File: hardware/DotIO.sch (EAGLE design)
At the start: 37 parts, among them CN1 1X4-BIG, U1 ATMEGA328P-MU-QFN32, X1 S4B-ZR, X2 S4B-ZR, X3 S4B-ZR, X4 S4B-ZR, X5 S4B-ZR, X6 S4B-ZR, X7 S4B-ZR

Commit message: Initial routing
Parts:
- removed LED5, LED6, LED7, LED8: (no value), SparkFun:LED0603
- removed X2: S4B-ZR, con-jst:S4B-ZR
- added C1, C9: 1uF, rcl:C-EUC0603
- added D1, D2: (no value), diode:DIODE-SOD523
- added IC2: (no value), MCP1700:MCP1700TT
- added J3: USB-MICROB, SparkFun-Retired:USB-MICROB
- added R6: 68Ω, rcl:R-EU_R0603
- added R8: 1.5kΩ, rcl:R-EU_R0603
- R2: value 150Ω -> 68Ω; device SparkFun:RESISTOR-ARRAY0603-ARV -> rcl:R-EU_R0603
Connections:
- net LED renamed RGB_RED
- removed net ADCENA: U1.PB1(OC1A/PCINT1)
- removed net CS_FLASH: U1.PC0(ADC0/PCINT8)
- removed net N$11: LED6.C, R2A.1
- removed net N$12: LED7.C, R2B.1
- removed net N$13: LED8.C, R2D.1
- removed net N$3: LED5.C, R2C.1
- removed net OUTA: LED11.A, LED3.A, LED5.A, LED6.A, U1.PB2(SS/OC1B/PCINT2), X1-3.1, X2-3.1, X3-3.1, X5-3.1
- removed net OUTB: LED12.A, LED4.A, LED7.A, LED8.A, X1-2.1, X2-2.1, X3-2.1, X5-2.1
- removed net RSEL: U1.PC3(ADC3/PCINT11)
- removed net RXD: R1C.1
- removed net TXD: R1B.1
- new net 4_0: LED11.A, U1.PC0(ADC0/PCINT8), X5-3.1
- new net 4_1: LED12.A, U1.PC1(ADC1PCINT9), X5-2.1
- new net 5_0: LED3.A, U1.PC2(ADC2PCINT10), X3-3.1
- new net 5_1: LED4.A, U1.PC3(ADC3/PCINT11), X3-2.1
- new net RGB_BLUE: R1C.1, U1.PB2(SS/OC1B/PCINT2)
- new net RGB_GREEN: R1B.1, U1.PB1(OC1A/PCINT1)
- new net USB_D+: D2.C, J3.D+, R2.1
- new net USB_D-: D1.C, J3.D-, R6.1, R8.1
- net +3V3: now also C1.1, IC2.OUT, R8.2, X1-3.1
- net +5V: now also C9.1, IC2.IN, J3.VBUS; no longer X1-4.1, X2-4.1
- net D+: now also R2.2; no longer U1.PC2(ADC2PCINT10)
- net D-: now also R6.2; no longer U1.PC1(ADC1PCINT9)
- net GND: now also C1.2, C9.2, D1.A, D2.A, IC2.GND, J3.GND, X1-4.1; no longer R2A.2, R2B.2, R2C.2, R2D.2, X1-1.1, X2-1.1
- net SCL: now also X1-2.1
- net SDA: now also X1-1.1
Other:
- moved on the sheet: X1-1, X1-2, X1-3, X1-4

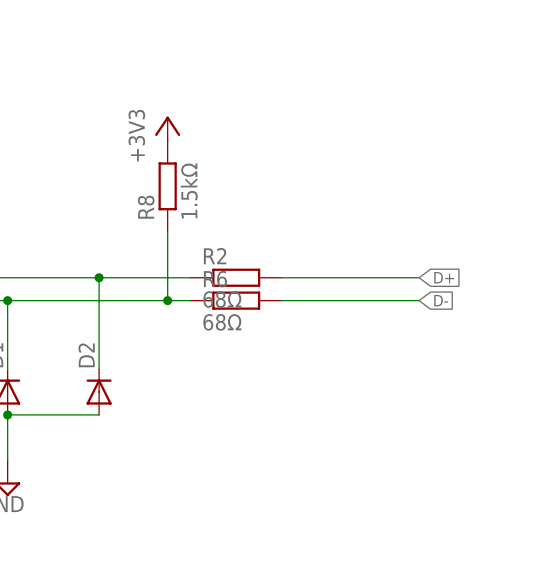
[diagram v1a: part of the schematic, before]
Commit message: Bind USB to SPI pins
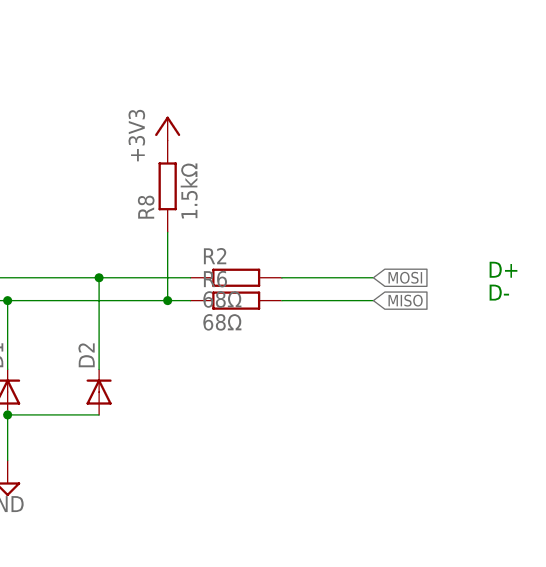
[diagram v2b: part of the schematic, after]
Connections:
- removed net D+: R2.2
- removed net D-: R6.2
- net MISO: now also R6.2
- net MOSI: now also R2.2
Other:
- note added: "D+"
- note added: "D-"
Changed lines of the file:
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@@
 <setting verticaltext="up"/>
 </settings>
-<grid distance="0.05" unitdist="inch" unit="inch" style="lines" multiple="1" display="no" altdistance="0.01" altunitdist="inch" altunit="inch"/>
+<grid distance="0.1" unitdist="inch" unit="inch" style="lines" multiple="1" display="no" altdistance="0.01" altunitdist="inch" altunit="inch"/>
 <layers>
 <layer number="1" name="Top" color="4" fill="1" visible="no" active="no"/>
@@
 <text x="196.85" y="213.36" size="1.778" layer="91">white</text>
 <text x="196.85" y="203.2" size="1.778" layer="91">red</text>
+<text x="381" y="144.78" size="1.778" layer="91">D+</text>
+<text x="381" y="142.24" size="1.778" layer="91">D-</text>
 </plain>
 <instances>
@@
 <label x="52.07" y="125.73" size="1.27" layer="95" rot="R180" xref="yes"/>
 </segment>
+<segment>
+<pinref part="R2" gate="G$1" pin="2"/>
+<wire x1="358.14" y1="144.78" x2="368.3" y2="144.78" width="0.1524" layer="91"/>
+<label x="368.3" y="144.78" size="1.27" layer="95" xref="yes"/>
+</segment>
 </net>
 <net name="MISO" class="0">
@@
 <wire x1="60.96" y1="123.19" x2="52.07" y2="123.19" width="0.1524" layer="91"/>
 <label x="52.07" y="123.19" size="1.27" layer="95" rot="R180" xref="yes"/>
+</segment>
+<segment>
+<pinref part="R6" gate="G$1" pin="2"/>
+<wire x1="358.14" y1="142.24" x2="368.3" y2="142.24" width="0.1524" layer="91"/>
+<label x="368.3" y="142.24" size="1.27" layer="95" xref="yes"/>
 </segment>
 </net>
@@
 </segment>
 </net>
-<net name="D-" class="0">
-<segment>
-<pinref part="R6" gate="G$1" pin="2"/>
-<wire x1="358.14" y1="142.24" x2="373.38" y2="142.24" width="0.1524" layer="91"/>
-<label x="373.38" y="142.24" size="1.27" layer="95" xref="yes"/>
-</segment>
-</net>
-<net name="D+" class="0">
-<segment>
-<pinref part="R2" gate="G$1" pin="2"/>
-<wire x1="358.14" y1="144.78" x2="373.38" y2="144.78" width="0.1524" layer="91"/>
-<label x="373.38" y="144.78" size="1.27" layer="95" xref="yes"/>
-</segment>
-</net>

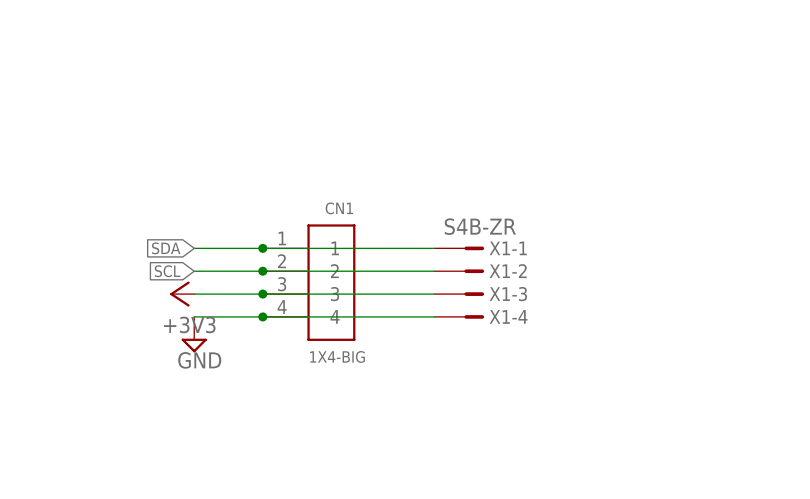
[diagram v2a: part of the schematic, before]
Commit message: Flip I2C JST port
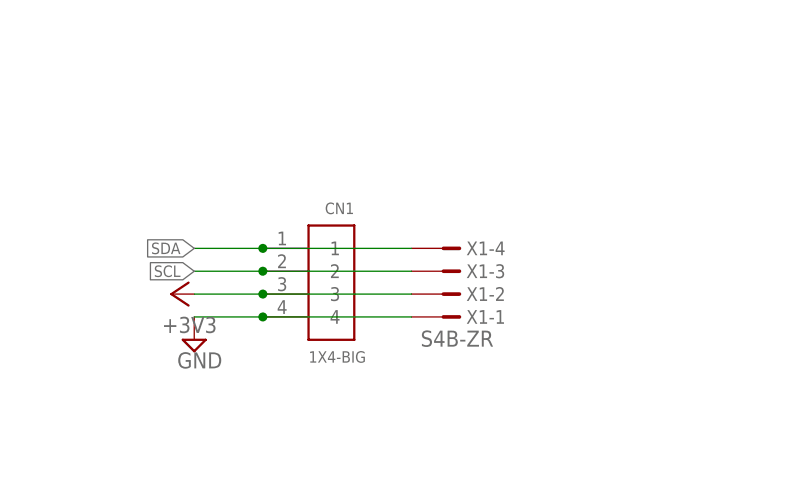
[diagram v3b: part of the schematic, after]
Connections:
- net +3V3: now also X1-2.1; no longer X1-3.1
- net GND: now also X1-1.1; no longer X1-4.1
- net SCL: now also X1-3.1; no longer X1-2.1
- net SDA: now also X1-4.1; no longer X1-1.1
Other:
- moved on the sheet: X1-1, X1-2, X1-3, X1-4
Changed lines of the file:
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@@
 <setting verticaltext="up"/>
 </settings>
-<grid distance="0.1" unitdist="inch" unit="inch" style="lines" multiple="1" display="no" altdistance="0.01" altunitdist="inch" altunit="inch"/>
+<grid distance="0.05" unitdist="inch" unit="inch" style="lines" multiple="1" display="no" altdistance="0.01" altunitdist="inch" altunit="inch"/>
 <layers>
 <layer number="1" name="Top" color="4" fill="1" visible="no" active="no"/>
@@
 <instance part="SUPPLY10" gate="GND" x="269.24" y="88.9"/>
 <instance part="J3" gate="G$1" x="279.4" y="99.06"/>
-<instance part="X1" gate="-1" x="100.33" y="-72.39"/>
-<instance part="X1" gate="-2" x="100.33" y="-74.93"/>
-<instance part="X1" gate="-3" x="100.33" y="-77.47"/>
-<instance part="X1" gate="-4" x="100.33" y="-80.01"/>
+<instance part="X1" gate="-1" x="97.79" y="-80.01" rot="MR180"/>
+<instance part="X1" gate="-2" x="97.79" y="-77.47" rot="MR180"/>
+<instance part="X1" gate="-3" x="97.79" y="-74.93" rot="MR180"/>
+<instance part="X1" gate="-4" x="97.79" y="-72.39" rot="MR180"/>
 </instances>
 <busses>
@@
 <wire x1="76.2" y1="-80.01" x2="68.58" y2="-80.01" width="0.1524" layer="91"/>
 <pinref part="SUPPLY11" gate="GND" pin="GND"/>
-<pinref part="X1" gate="-4" pin="1"/>
-<wire x1="76.2" y1="-80.01" x2="95.25" y2="-80.01" width="0.1524" layer="91"/>
+<pinref part="X1" gate="-1" pin="1"/>
+<wire x1="92.71" y1="-80.01" x2="76.2" y2="-80.01" width="0.1524" layer="91"/>
 <junction x="76.2" y="-80.01"/>
 </segment>
@@
 <wire x1="76.2" y1="-72.39" x2="68.58" y2="-72.39" width="0.1524" layer="91"/>
 <label x="68.58" y="-72.39" size="1.27" layer="95" rot="R180" xref="yes"/>
-<pinref part="X1" gate="-1" pin="1"/>
-<wire x1="76.2" y1="-72.39" x2="95.25" y2="-72.39" width="0.1524" layer="91"/>
+<pinref part="X1" gate="-4" pin="1"/>
+<wire x1="92.71" y1="-72.39" x2="76.2" y2="-72.39" width="0.1524" layer="91"/>
 <junction x="76.2" y="-72.39"/>
 </segment>
@@
 <wire x1="76.2" y1="-77.47" x2="68.58" y2="-77.47" width="0.1524" layer="91"/>
 <pinref part="+3V7" gate="G$1" pin="+3V3"/>
-<pinref part="X1" gate="-3" pin="1"/>
-<wire x1="76.2" y1="-77.47" x2="95.25" y2="-77.47" width="0.1524" layer="91"/>
+<pinref part="X1" gate="-2" pin="1"/>
+<wire x1="92.71" y1="-77.47" x2="76.2" y2="-77.47" width="0.1524" layer="91"/>
 <junction x="76.2" y="-77.47"/>
 </segment>
@@
 <wire x1="76.2" y1="-74.93" x2="68.58" y2="-74.93" width="0.1524" layer="91"/>
 <label x="68.58" y="-74.93" size="1.27" layer="95" rot="R180" xref="yes"/>
-<pinref part="X1" gate="-2" pin="1"/>
-<wire x1="76.2" y1="-74.93" x2="95.25" y2="-74.93" width="0.1524" layer="91"/>
+<pinref part="X1" gate="-3" pin="1"/>
+<wire x1="92.71" y1="-74.93" x2="76.2" y2="-74.93" width="0.1524" layer="91"/>
 <junction x="76.2" y="-74.93"/>
 </segment>
